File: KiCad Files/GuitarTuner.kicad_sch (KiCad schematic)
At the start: 10 parts, among them J1 AudioJack2_Switch, J2 AudioJack3_Switch, U1 TL072

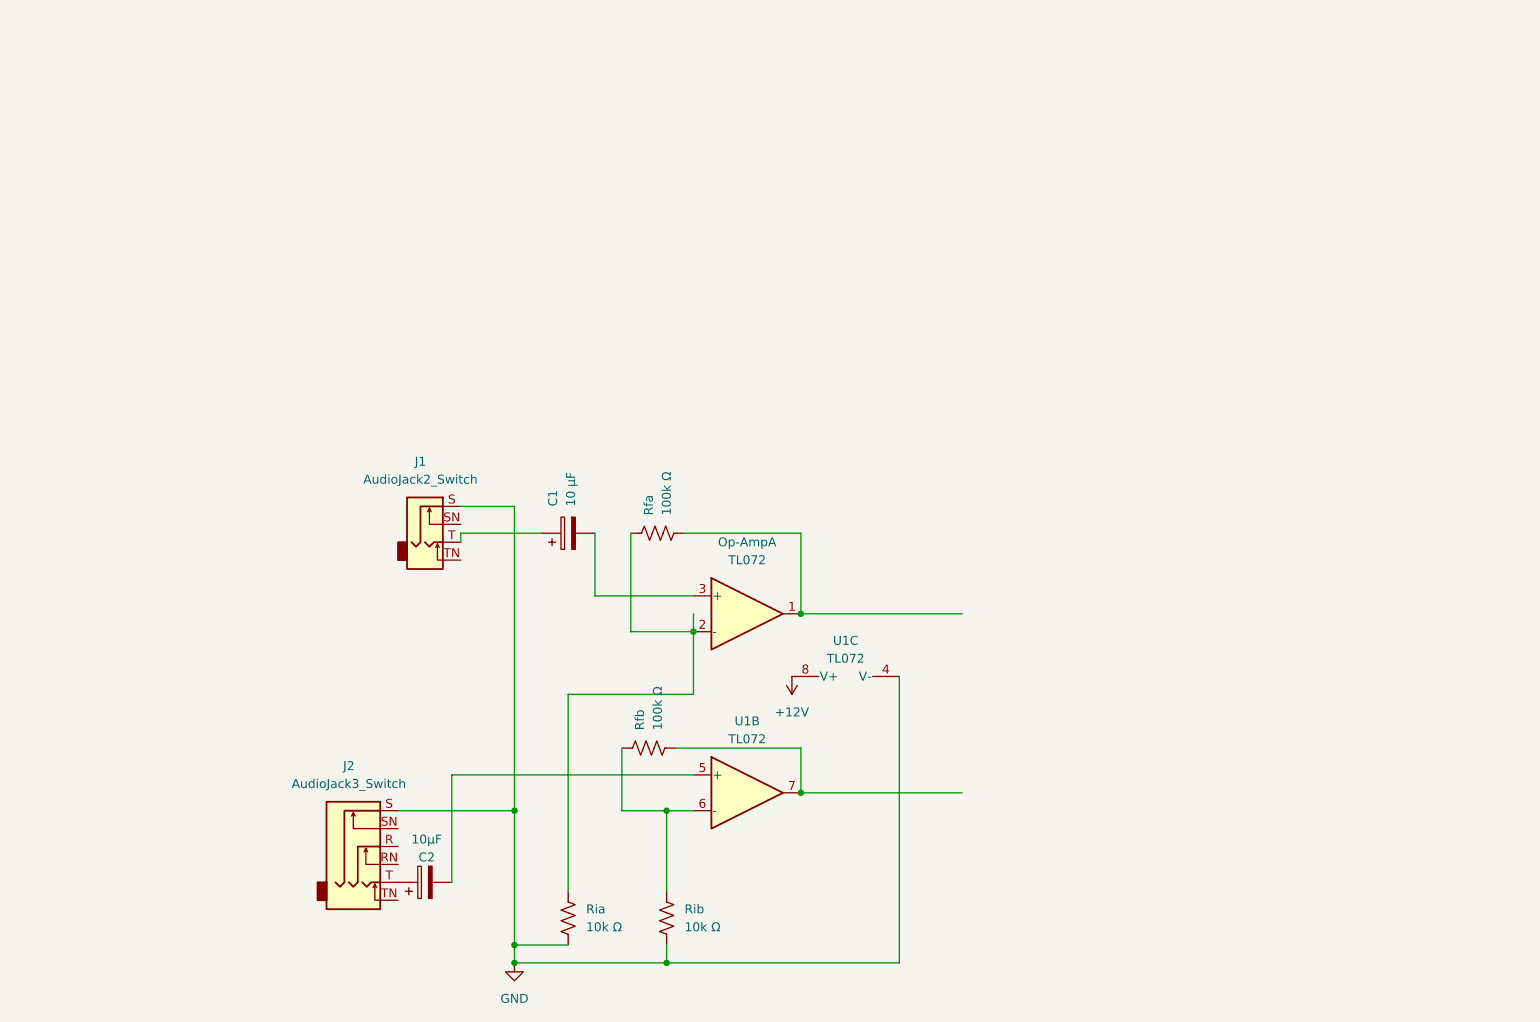
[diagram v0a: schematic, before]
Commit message: elec. circuit schem done
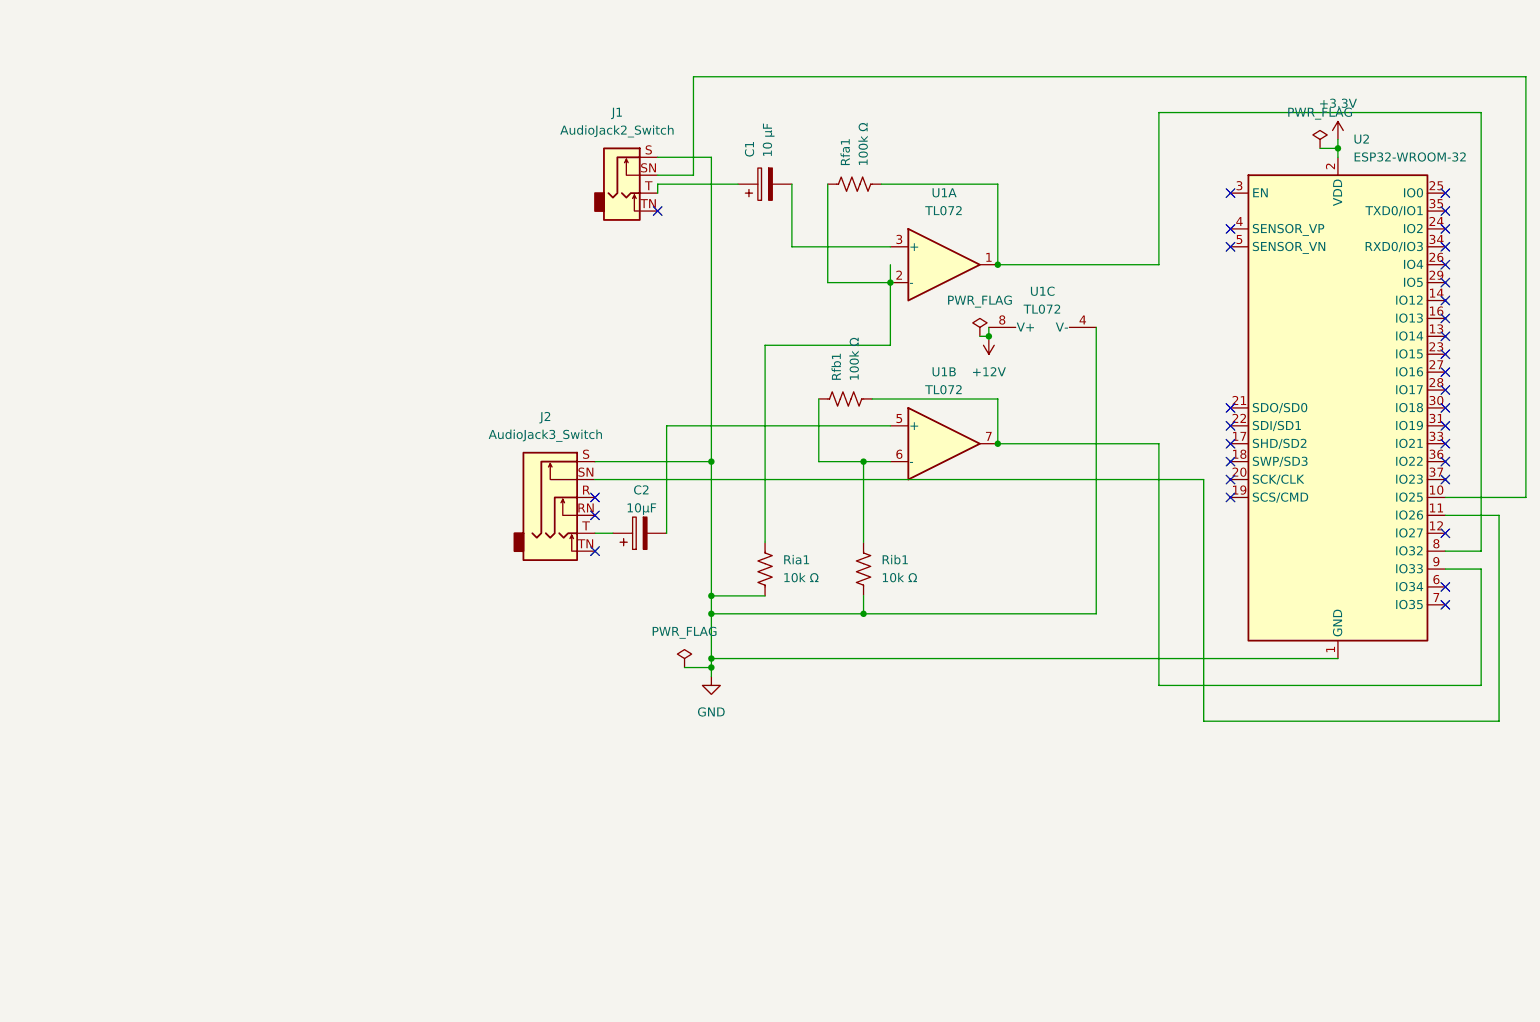
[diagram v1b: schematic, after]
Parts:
- added U2: ESP32-WROOM-32, RF_Module:ESP32-WROOM-32, symbol RF_Module:ESP32-WROOM-32
- C2: renamed from 10µF; value C2 -> 10µF
- renumbered Rfa to Rfa1, Rfb to Rfb1, Ria to Ria1, Rib to Rib1, Op-Amp to U1
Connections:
- net GND: now also U2.1 (GND), U2.15 (GND), U2.38 (GND), U2.39 (GND)
- net at Rfb1.2, U1.7: now also U2.9 (IO33)
- net at Rfa1.2, U1.1: now also U2.8 (IO32)
- net at J2.SN: now also U2.11 (IO26)
- net at J1.SN: now also U2.10 (IO25)
- new net +3.3V: U2.2 (VDD)
- no-connect marks 0 -> 33
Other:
- moved on the sheet: C1, C2, J1, J2, Rfa1, Rfb1, Ria1, Rib1, U1A, U1B, U1C

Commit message: circuit schematic
added oled and audio output
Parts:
- added DS1: OLED-128O064D, Display:OLED-128O064D, symbol Display_Graphic:OLED-128O064D
- added J3: AudioJack2, symbol Connector_Audio:AudioJack2
- C1: footprint Capacitor_SMD:CP_Elec_5x3 -> Package_SO:SOIC-8_3.9x4.9mm_P1.27mm
- C2: footprint (none) -> Capacitor_SMD:CP_Elec_5x3
- J1: footprint (none) -> Connector_Audio:Jack_6.35mm_Neutrik_NMJ4HCD2_Horizontal
- J2: footprint (none) -> Connector_Audio:Jack_3.5mm_CUI_SJ-3523-SMT_Horizontal
- Rfa1, Rfb1, Ria1, Rib1: footprint (none) -> Resistor_SMD:R_0805_2012Metric_Pad1.20x1.40mm_HandSolder
- U1: footprint (none) -> Package_SO:SOIC-8_3.9x4.9mm_P1.27mm
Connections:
- net GND: now also DS1.1 (GND), DS1.30 (GND), J3.S
- net at U2.12 (IO27): now also J3.T
- no-connect marks 33 -> 32
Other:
- moved on the sheet: C1, C2, J1, J2, Rfa1, Rfb1, Ria1, Rib1, U1A, U1B, U1C, U2
